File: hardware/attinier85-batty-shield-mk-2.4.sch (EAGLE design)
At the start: 5 parts, among them U1 ATTINIEST85_SHIELDV2

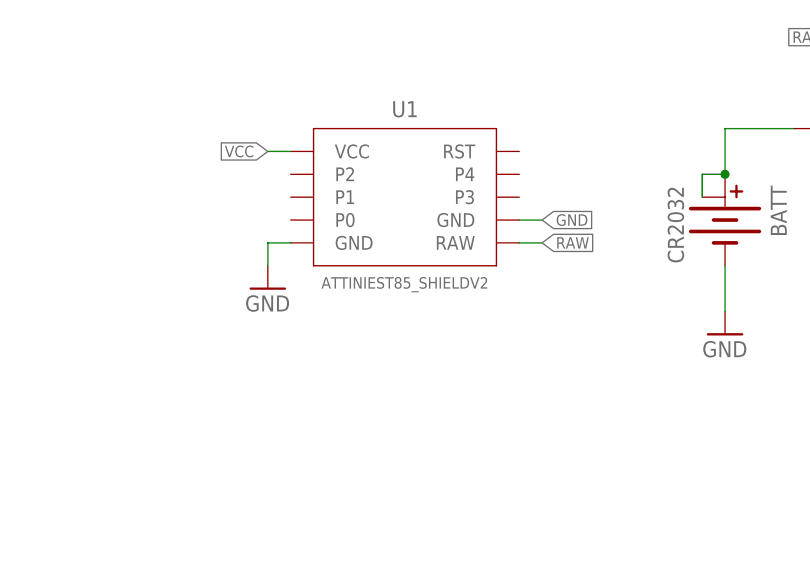
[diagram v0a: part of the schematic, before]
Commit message: renaming parts
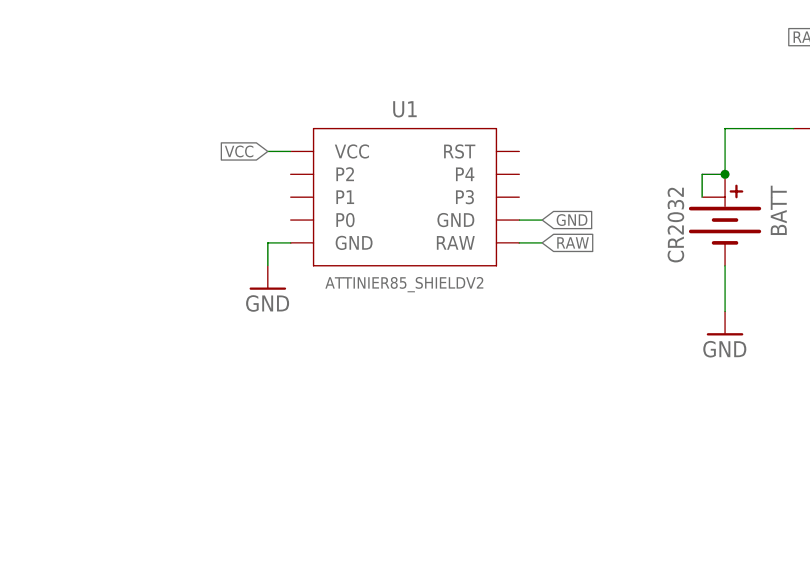
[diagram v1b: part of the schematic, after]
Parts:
- U1: value ATTINIEST85_SHIELDV2 -> ATTINIER85_SHIELDV2; device A_butts:ATTINIEST85_SHIELDV2 -> A_butts:ATTINIER85_SHIELDV2
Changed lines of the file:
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@@
 <parts>
 <part name="FRAME1" library="A_butts" deviceset="FRAME-LETTER" device="NO_PACKAGE"/>
-<part name="U1" library="A_butts" deviceset="ATTINIEST85_SHIELD" device="V2"/>
+<part name="U1" library="A_butts" deviceset="ATTINIER85_SHIELD" device="V2"/>
 <part name="GND1" library="A_butts" deviceset="GND" device=""/>
 <part name="BATT" library="A_butts" deviceset="BATTERY-COIN" device="CR2032_SMD" value="CR2032"/>
